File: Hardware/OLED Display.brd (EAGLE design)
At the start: 44.4 x 12.7 mm, 27 parts, among them J1 QWIIC_RIGHT_ANGLE, J3 QWIIC_RIGHT_ANGLE, U2 APX803S-SA, U3 OLED_0.9"-QG-2832TLBFG02

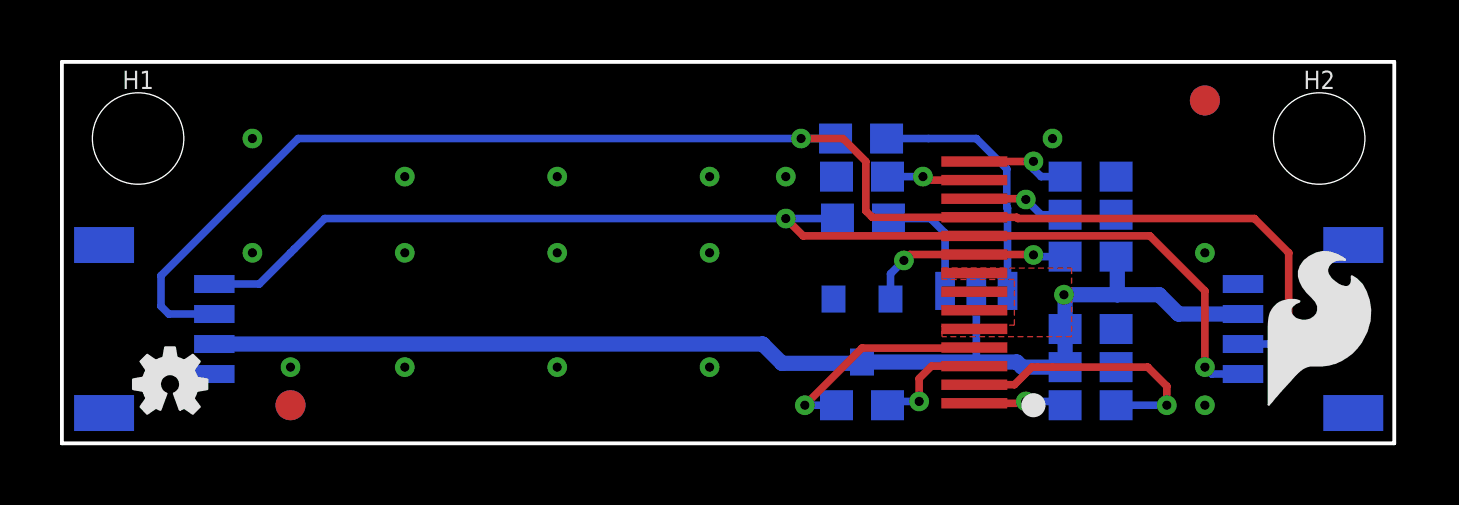
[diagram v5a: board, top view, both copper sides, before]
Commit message: Updates the display device and footprint name, adds version in silk
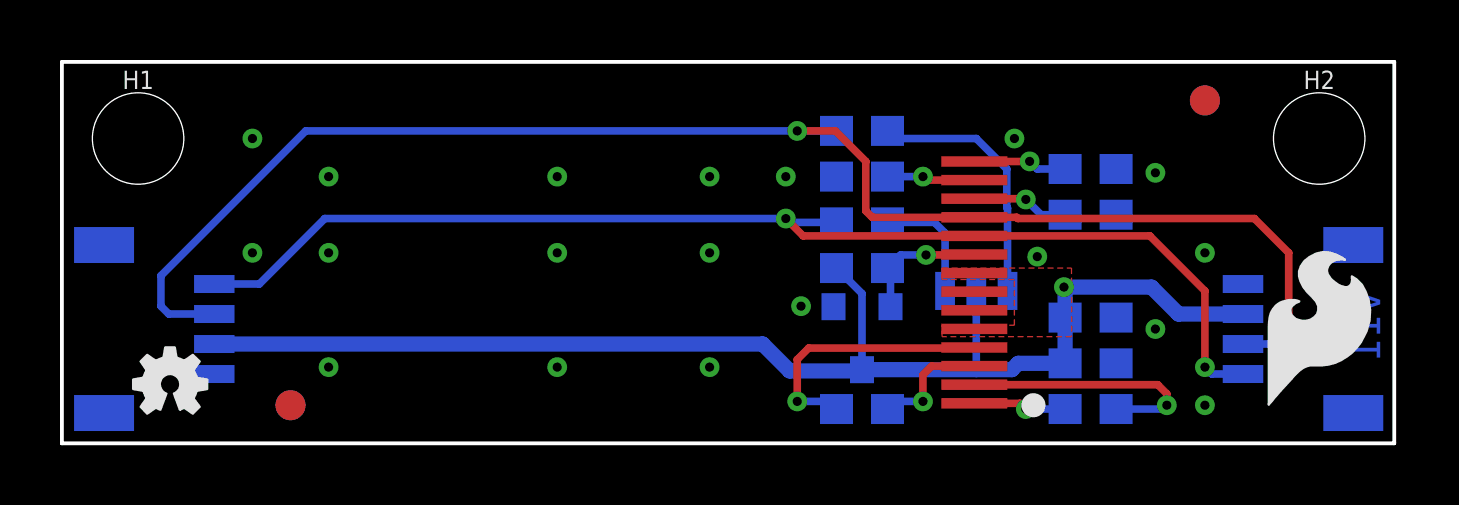
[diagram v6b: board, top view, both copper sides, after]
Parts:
- added U$2: (no value), prod:OLED_DISPLAY94
- added U$3: (no value), prod:128X3295
- U3: value OLED_0.9"-QG-2832TLBFG02 -> QG-2832TLBFG02; device Module:OLED-12832 -> Module:QG-2832TLBFG02
- moved R4 7.63 mm to (26.7, 5.84), turned to 0 degrees
- moved LOGO1 5.24 mm to (15.2, 7.62)
- moved C4 0.38 mm to (34.3, 4.19)
- moved R2 0.26 mm to (26.7, 10.4)
- moved U2 0.25 mm to (26.7, 3.56)
- moved C7 0.25 mm to (34.3, 9.14)
- moved R1 0.13 mm to (26.7, 7.37)
- moved C1 0.13 mm to (26.7, 1.14)
- moved C2 0.13 mm to (34.3, 1.14)
- moved C8 0.13 mm to (34.3, 2.67)
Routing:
- net 3.3V: track 41.0 -> 44.2 mm
- net RST: track 6.96 -> 4.41 mm, vias 2 -> 1
- net N$2: track 7.50 -> 8.88 mm
- net N$17: track 9.25 -> 8.67 mm
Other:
- board text added: "1.6mm Thickness 1 oz. Copper Lead-Free HASL finish Material: TG135-140 Red Soldermask White Silkscreen"
- board text added: "v11"

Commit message: Adds label to I2C jumper
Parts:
- added U$4: (no value), bot:#I2C#16
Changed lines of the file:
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@@
 <element name="U$2" library="prod" package="OLED_DISPLAY94" value="" x="15.24" y="5.08" smashed="yes" rot="MR0"/>
 <element name="U$3" library="prod" package="128X3295" value="" x="15.24" y="3.81" smashed="yes" rot="MR0"/>
+<element name="U$4" library="bot" package="#I2C#16" value="" x="30.607" y="6.604" smashed="yes" rot="MR0"/>
 </elements>
 <signals>

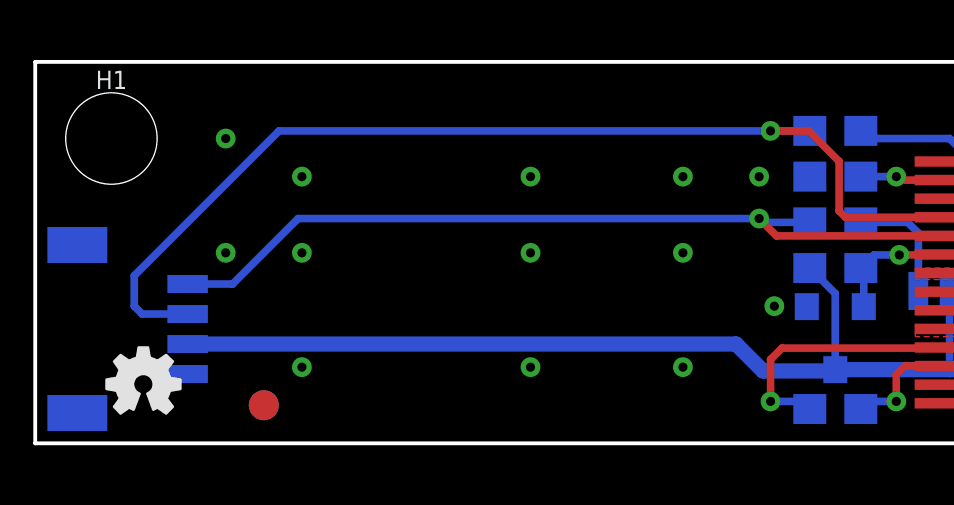
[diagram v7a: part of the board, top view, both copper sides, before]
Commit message: Adds testpoints
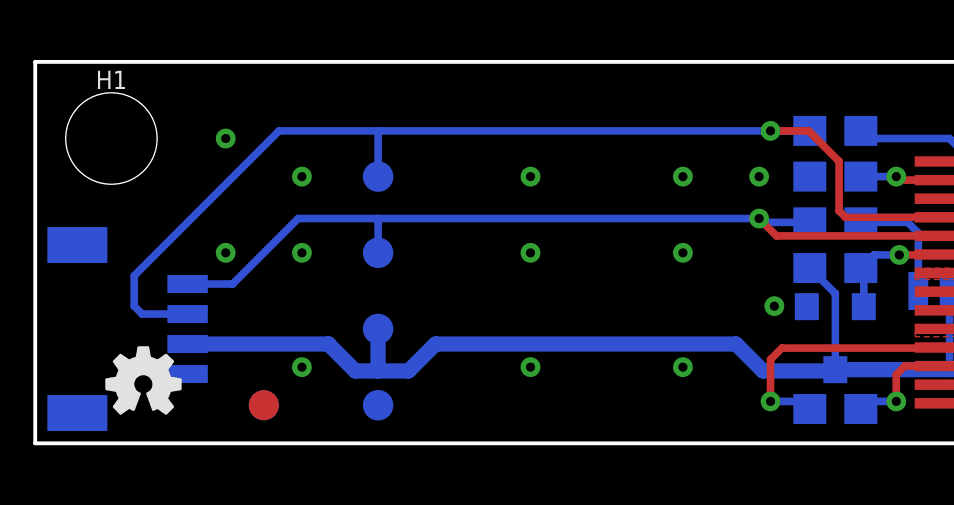
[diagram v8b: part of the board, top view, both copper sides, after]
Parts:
- added TP1, TP2, TP3, TP4: TEST-POINT3X4, SparkFun-Connectors:PAD.03X.04
- moved LOGO1 2.54 mm to (17.8, 7.62)
- moved U$2 2.54 mm to (17.8, 5.08)
- moved U$3 2.54 mm to (17.8, 3.81)
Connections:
- net 3.3V: now also TP3.1
- net GND: now also TP4.1
- net SCL: now also TP1.1
- net SDA: now also TP2.1
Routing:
- net 3.3V: track 44.2 -> 46.3 mm
- net SDA: track 50.8 -> 52.3 mm
- net SCL: track 40.6 -> 41.7 mm
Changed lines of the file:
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@@
 <layer number="37" name="tTest" color="7" fill="1" visible="no" active="yes"/>
 <layer number="38" name="bTest" color="7" fill="1" visible="no" active="yes"/>
-<layer number="39" name="tKeepout" color="4" fill="11" visible="yes" active="yes"/>
-<layer number="40" name="bKeepout" color="1" fill="11" visible="yes" active="yes"/>
-<layer number="41" name="tRestrict" color="4" fill="10" visible="yes" active="yes"/>
+<layer number="39" name="tKeepout" color="4" fill="11" visible="no" active="yes"/>
+<layer number="40" name="bKeepout" color="1" fill="11" visible="no" active="yes"/>
+<layer number="41" name="tRestrict" color="4" fill="10" visible="no" active="yes"/>
 <layer number="42" name="bRestrict" color="1" fill="10" visible="no" active="yes"/>
 <layer number="43" name="vRestrict" color="2" fill="10" visible="no" active="yes"/>
@@
 <attribute name="VALUE" x="28.321" y="3.556" size="0.6096" layer="28" font="vector" ratio="20" rot="MR270" align="top-center"/>
 </element>
-<element name="LOGO1" library="SparkFun-Aesthetics" package="SFE_LOGO_NAME_FLAME_.1" value="SFE_LOGO_NAME_FLAME.1_INCH" x="15.24" y="7.62" smashed="yes" rot="MR0"/>
+<element name="LOGO1" library="SparkFun-Aesthetics" package="SFE_LOGO_NAME_FLAME_.1" value="SFE_LOGO_NAME_FLAME.1_INCH" x="17.78" y="7.62" smashed="yes" rot="MR0"/>
 <element name="U$1" library="SparkFun-Aesthetics" package="SFE_LOGO_FLAME_.2" value="" x="41.91" y="3.81" smashed="yes"/>
 <element name="U3" library="Module" package="QG-2832TLBFG02" value="QG-2832TLBFG02" x="30.48" y="5.08" smashed="yes">
@@
 <attribute name="VALUE" x="28.702" y="0.127" size="0.6096" layer="27" font="vector" ratio="20"/>
 </element>
-<element name="U$2" library="prod" package="OLED_DISPLAY94" value="" x="15.24" y="5.08" smashed="yes" rot="MR0"/>
-<element name="U$3" library="prod" package="128X3295" value="" x="15.24" y="3.81" smashed="yes" rot="MR0"/>
+<element name="U$2" library="prod" package="OLED_DISPLAY94" value="" x="17.78" y="5.08" smashed="yes" rot="MR0"/>
+<element name="U$3" library="prod" package="128X3295" value="" x="17.78" y="3.81" smashed="yes" rot="MR0"/>
 <element name="U$4" library="bot" package="#I2C#16" value="" x="30.607" y="6.604" smashed="yes" rot="MR0"/>
+<element name="TP1" library="SparkFun-Connectors" package="PAD.03X.04" value="TEST-POINT3X4" x="11.43" y="6.35" smashed="yes" rot="MR0"/>
+<element name="TP2" library="SparkFun-Connectors" package="PAD.03X.04" value="TEST-POINT3X4" x="11.43" y="8.89" smashed="yes" rot="MR0"/>
+<element name="TP3" library="SparkFun-Connectors" package="PAD.03X.04" value="TEST-POINT3X4" x="11.43" y="3.81" smashed="yes" rot="MR0"/>
+<element name="TP4" library="SparkFun-Connectors" package="PAD.03X.04" value="TEST-POINT3X4" x="11.43" y="1.27" smashed="yes" rot="MR0"/>
 </elements>
 <signals>
@@
 <via x="24.638" y="4.572" extent="1-16" drill="0.3048"/>
 <via x="32.512" y="6.223" extent="1-16" drill="0.3048"/>
+<contactref element="TP4" pad="1"/>
 </signal>
 <signal name="SCL">
@@
 <wire x1="6.58" y1="5.31" x2="5.08" y2="5.31" width="0.254" layer="16"/>
 <wire x1="6.58" y1="5.31" x2="8.763" y2="7.493" width="0.254" layer="16"/>
-<wire x1="8.763" y1="7.493" x2="24.13" y2="7.493" width="0.254" layer="16"/>
+<wire x1="8.763" y1="7.493" x2="11.43" y2="7.493" width="0.254" layer="16"/>
+<wire x1="11.43" y1="7.493" x2="24.13" y2="7.493" width="0.254" layer="16"/>
 <wire x1="25.82" y1="7.366" x2="24.257" y2="7.366" width="0.254" layer="16"/>
 <wire x1="24.13" y1="7.493" x2="24.257" y2="7.366" width="0.254" layer="16"/>
@@
 <wire x1="24.709" y1="6.914" x2="24.13" y2="7.493" width="0.254" layer="1"/>
 <via x="24.13" y="7.493" extent="1-16" drill="0.3048"/>
+<contactref element="TP1" pad="1"/>
+<wire x1="11.43" y1="7.493" x2="11.43" y2="6.35" width="0.254" layer="16"/>
 </signal>
 <signal name="SDA">
@@
 <wire x1="8.128" y1="10.414" x2="3.302" y2="5.588" width="0.254" layer="16"/>
 <wire x1="25.82" y1="10.414" x2="24.511" y2="10.414" width="0.254" layer="16"/>
-<wire x1="24.511" y1="10.414" x2="8.128" y2="10.414" width="0.254" layer="16"/>
+<wire x1="24.511" y1="10.414" x2="11.43" y2="10.414" width="0.254" layer="16"/>
+<wire x1="11.43" y1="10.414" x2="8.128" y2="10.414" width="0.254" layer="16"/>
 <wire x1="27.01" y1="7.534" x2="26.797" y2="7.747" width="0.254" layer="1"/>
 <via x="24.511" y="10.414" extent="1-16" drill="0.3048"/>
@@
 <wire x1="25.781" y1="10.414" x2="24.511" y2="10.414" width="0.254" layer="1"/>
 <wire x1="30.414" y1="7.534" x2="27.01" y2="7.534" width="0.254" layer="1"/>
+<contactref element="TP2" pad="1"/>
+<wire x1="11.43" y1="10.414" x2="11.43" y2="8.89" width="0.254" layer="16"/>
 </signal>
 <signal name="N$6">
@@
 <contactref element="U3" pad="8"/>
 <contactref element="U3" pad="5"/>
-<wire x1="5.08" y1="3.31" x2="23.36" y2="3.31" width="0.508" layer="16"/>
+<wire x1="5.08" y1="3.31" x2="9.779" y2="3.31" width="0.508" layer="16"/>
+<wire x1="9.779" y1="3.31" x2="9.775" y2="3.306" width="0.508" layer="16"/>
+<wire x1="13.343" y1="3.31" x2="23.36" y2="3.31" width="0.508" layer="16"/>
 <wire x1="23.36" y1="3.31" x2="24.257" y2="2.413" width="0.508" layer="16"/>
 <wire x1="26.67" y1="2.456" x2="26.627" y2="2.413" width="0.508" layer="16"/>
@@
 <wire x1="26.67" y1="4.992" x2="26.67" y2="2.456" width="0.254" layer="16"/>
 <wire x1="30.48" y1="5.08" x2="30.48" y2="2.456" width="0.254" layer="16"/>
+<contactref element="TP3" pad="1"/>
+<wire x1="10.668" y1="2.413" x2="9.775" y2="3.306" width="0.508" layer="16"/>
+<wire x1="10.668" y1="2.413" x2="11.43" y2="2.413" width="0.508" layer="16"/>
+<wire x1="11.43" y1="2.413" x2="12.446" y2="2.413" width="0.508" layer="16"/>
+<wire x1="12.446" y1="2.413" x2="13.343" y2="3.31" width="0.508" layer="16"/>
+<wire x1="11.43" y1="3.81" x2="11.43" y2="2.413" width="0.508" layer="16"/>
+<wire x1="30.48" y1="5.08" x2="30.414" y2="5.674" width="0" layer="19" extent="1-16"/>
+<wire x1="30.414" y1="3.814" x2="30.48" y2="5.08" width="0" layer="19" extent="1-16"/>
 </signal>
 <signal name="N$1">
